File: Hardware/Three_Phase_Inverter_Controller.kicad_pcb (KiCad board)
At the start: 2 copper layers, 165.1 x 127 mm, 150 parts, among them J1 POWER, J2 HALL, J3 IN/I2C, J4 UART, J5 USB_B, J6 ISP, Q1 IXFN110N60P3, Q2 IXFN110N60P3, Q3 IXFN110N60P3, Q4 IXFN110N60P3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

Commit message: did more routing
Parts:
- JP1, JP2, JP3, JP4: footprint Pin_Headers:Pin_Header_Straight_2x01_Pitch2.00mm -> Pin_Headers:Pin_Header_Straight_2x01_Pitch2.54mm
- moved JP2 3.10 mm to (74.3, 144.1)
- moved JP3 3.10 mm to (74.3, 140.3)
- moved R5 3.10 mm to (81.9, 141.6)
- moved R6 3.10 mm to (81.9, 143.5)
- moved R10 3.10 mm to (86.4, 141.6)
- moved R11 3.10 mm to (86.4, 143.5)
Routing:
- net +5V: track 0.00 -> 202.3 mm, vias 0 -> 4
- net +12V_HLDP: track 49.7 -> 234.9 mm, vias 0 -> 4
- net /I2C_SCL: track 0.00 -> 99.1 mm, vias 0 -> 2
- net /I2C_SDA: track 0.00 -> 94.0 mm
- net GND: track 61.2 -> 153.9 mm, vias 0 -> 30
- net /BLU_VS: track 0.00 -> 86.3 mm, vias 0 -> 2
- net /YLW_VS: track 0.00 -> 84.7 mm, vias 0 -> 4
- net /YLW_DRVH_R: track 0.00 -> 82.7 mm, vias 0 -> 2
- net /CMD_CURR4: track 0.00 -> 82.6 mm
- net /CMD_CURR3: track 0.00 -> 81.4 mm
- net /GRN_VS: track 0.00 -> 80.3 mm, vias 0 -> 4
- net +5V_USB: track 0.00 -> 79.7 mm
- net /CMD_CURR2: track 0.00 -> 78.3 mm
- net /CMD_CURR1: track 0.00 -> 76.2 mm
- net /CMD_CURR0: track 0.00 -> 75.2 mm
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- added copper zone on B.Cu, net +5V
- added copper zone on F.Cu, net +5V
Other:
- board text added: "usb = 0.018" width"

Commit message: Finished initial board layout
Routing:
- net +5V: track 202.3 -> 577.4 mm, vias 4 -> 24
- net /ULED: track 11.5 -> 186.5 mm, vias 0 -> 12
- net /TXD: track 1.78 -> 107.4 mm, vias 0 -> 2
- net /BLU_DRVL_R: track 0.00 -> 105.0 mm, vias 0 -> 2
- net /RXD: track 4.89 -> 107.1 mm, vias 0 -> 2
- net /PE2: track 17.5 -> 95.7 mm, vias 0 -> 2
- net /SD: track 49.4 -> 126.8 mm, vias 0 -> 1
- net /POS_A: track 17.6 -> 93.9 mm, vias 0 -> 6
- net GND: track 153.9 -> 230.1 mm, vias 30 -> 61
- net /PE3: track 14.2 -> 89.9 mm
- net /POS_B: track 17.3 -> 90.8 mm, vias 0 -> 6
- net /POS_C: track 17.1 -> 87.9 mm, vias 0 -> 6
- net /BLU_DRVH_R: track 7.38 -> 68.4 mm, vias 0 -> 2
- net /GRN_DRVL_R: track 0.00 -> 56.5 mm
- net /GRN_DRVH_R: track 7.38 -> 51.7 mm, vias 0 -> 4
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- added copper zone on B.Cu, net GND
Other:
- board text removed: "usb = 0.018" width"

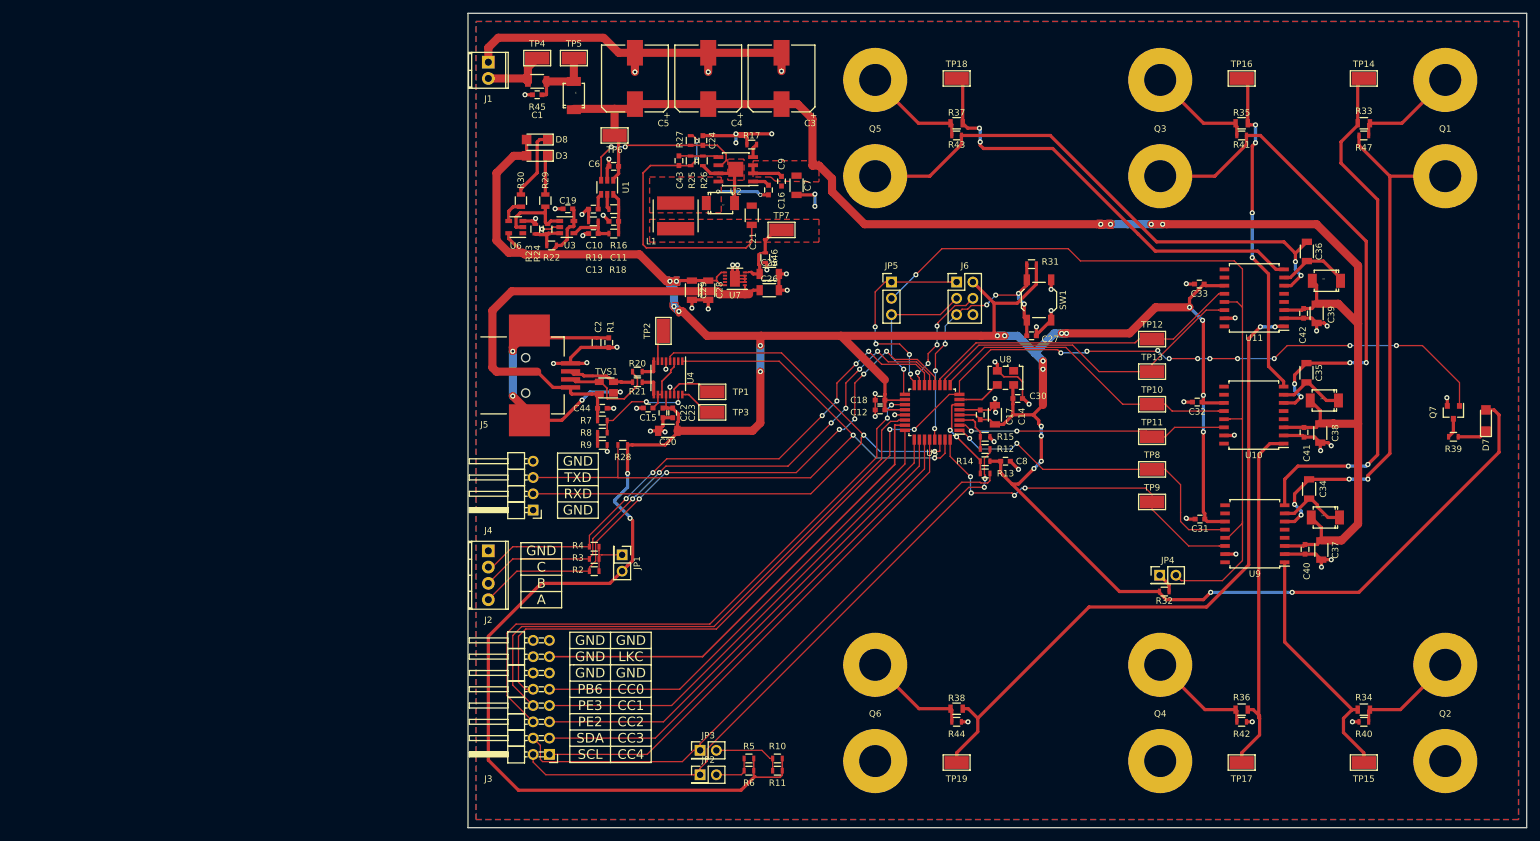
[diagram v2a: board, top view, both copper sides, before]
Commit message: Finished PCB, changed routing, regenerated schematic, generated gerbers
Put EXT_SHDN line in instead of ULED to external connector, changed
routing to reflect that. Added finishing touches to PCB silkscreen.
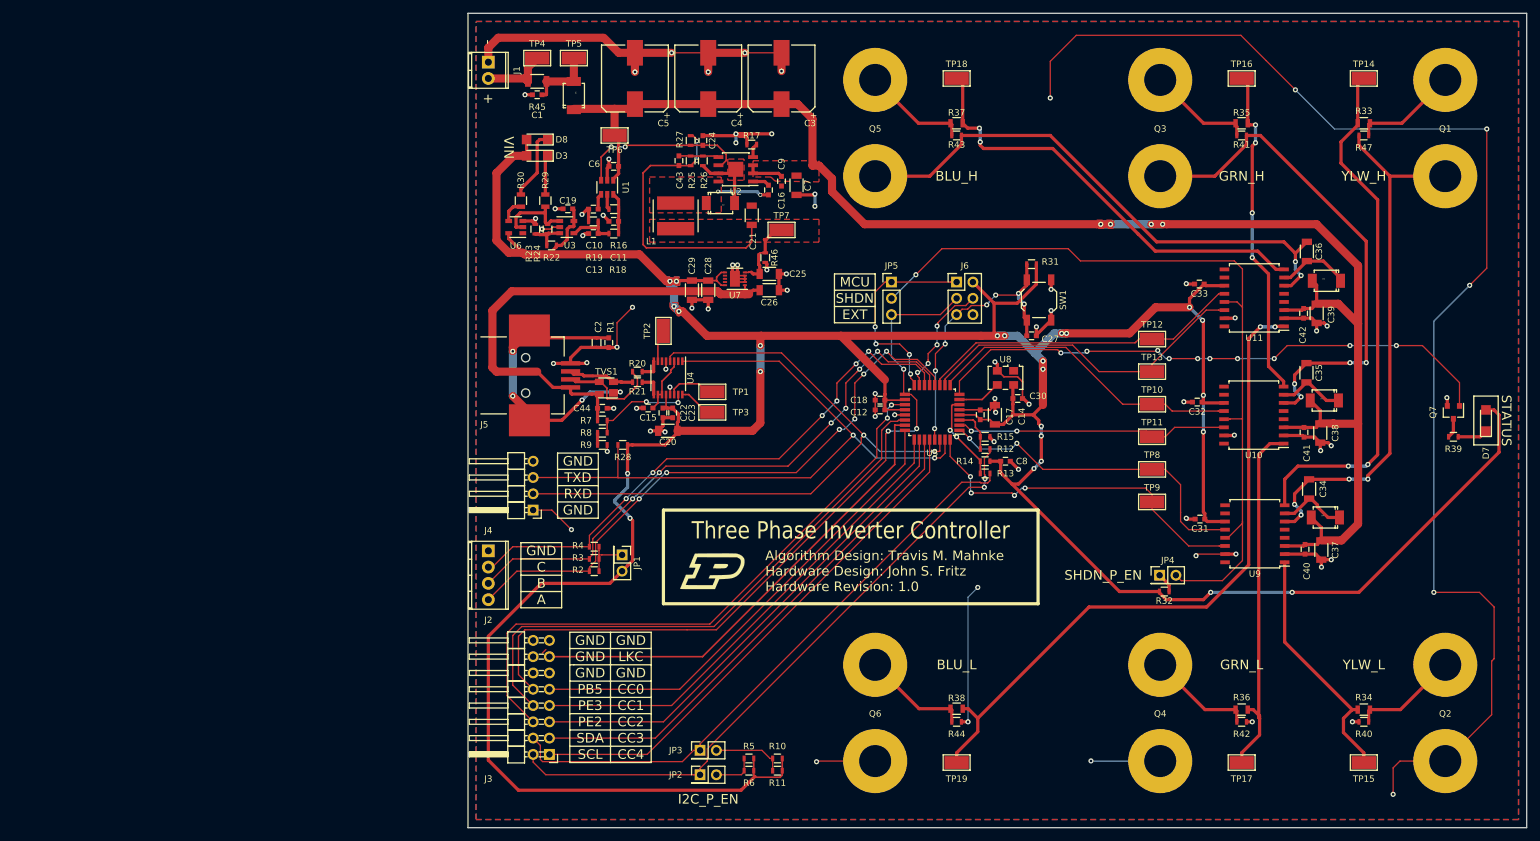
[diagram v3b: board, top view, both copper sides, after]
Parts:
- added G***: LOGO, Pictures:p, F.Cu at (76.2, 112.4)
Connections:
- J3 pad 10: /ULED -> /EX_SD/SCK
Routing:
- net GND: track 230.1 -> 498.2 mm, vias 61 -> 75
- net /ULED: track 186.5 -> 89.9 mm, vias 12 -> 10
- net /EX_SD/SCK: track 24.5 -> 118.4 mm, vias 1 -> 3
- net (no net): track 0.00 -> 0.83 mm
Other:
- board text added: "+"
- board text added: "-"
- board text added: "Algorithm Design: Travis M. Mahnke Hardware Design: John S. Fritz Hardware Revision: 1.0"
- board text added: "BLU_H"
- board text added: "BLU_L"
- board text added: "EXT"
- board text added: "GRN_H"
- board text added: "GRN_L"
- board text added: "I2C_P_EN"
- board text added: "MCU"
- board text added: "PB5"
- board text added: "SHDN"
- board text added: "SHDN_P_EN"
- board text added: "STATUS"
- board text added: "Three Phase Inverter Controller"
- board text added: "VIN"
- board text added: "YLW_H"
- board text added: "YLW_L"
- board text removed: "PB6"
